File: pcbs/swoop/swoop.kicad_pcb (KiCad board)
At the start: 2 copper layers, 109.5 x 89.6 mm, 68 parts, among them J1 TRRS, SW1 Choc, SW10 Choc, SW11 Choc, SW12 Choc, SW13 Choc, SW14 Choc, SW15 Choc, SW16 Choc, SW17 Choc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

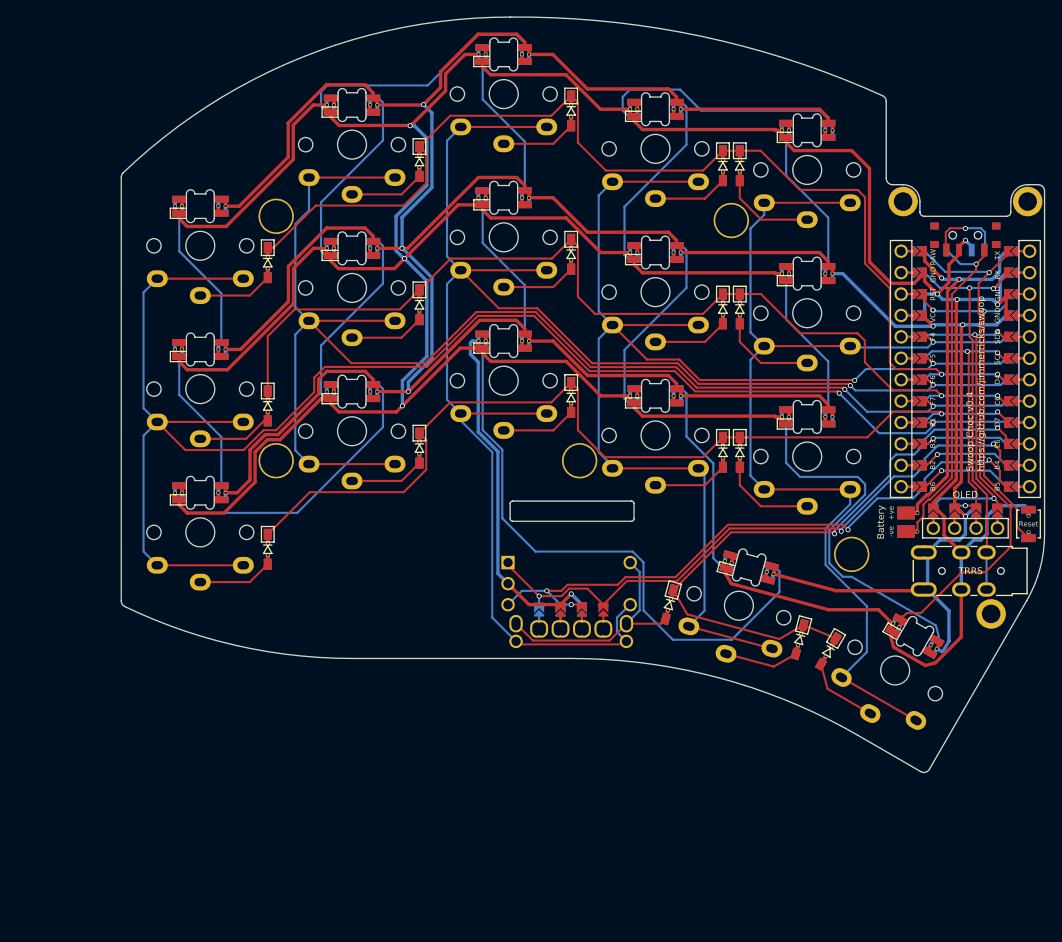
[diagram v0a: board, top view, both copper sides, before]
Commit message: Fixed the cover
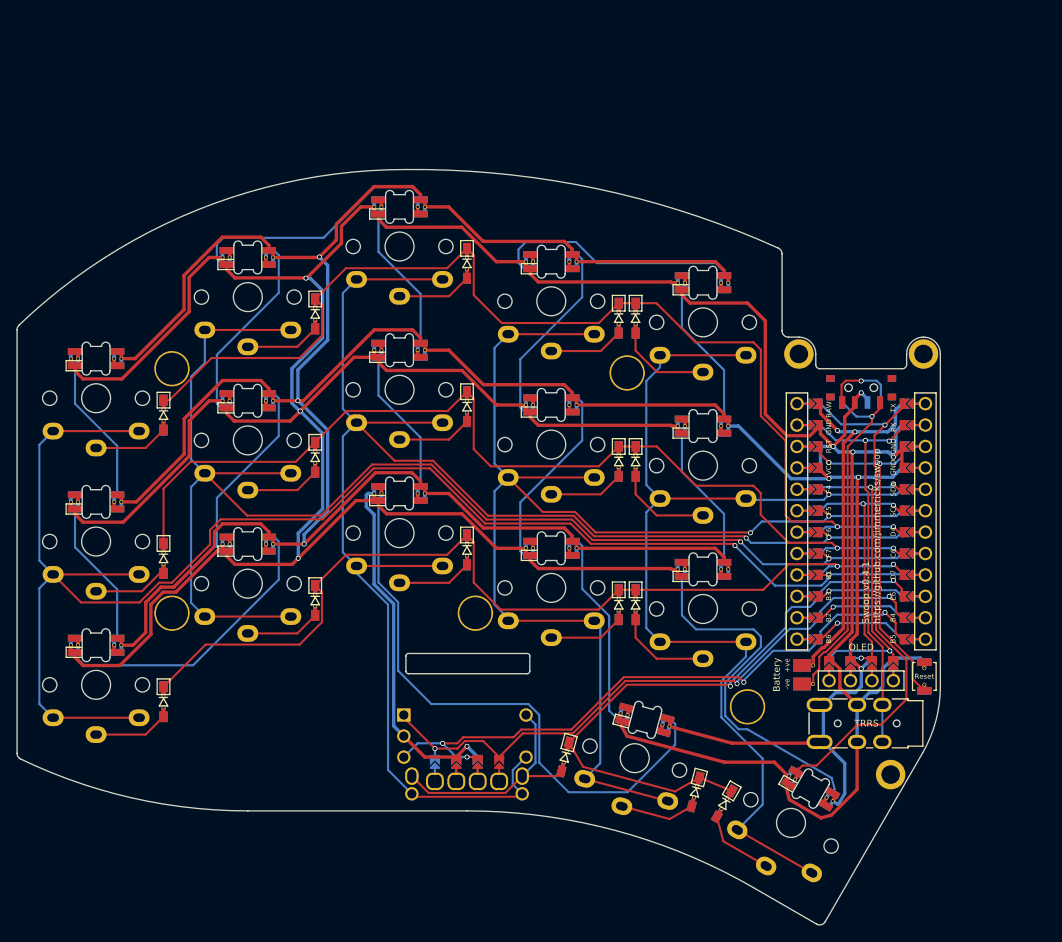
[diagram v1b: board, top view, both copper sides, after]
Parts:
- moved Ref** 22.5 mm to (165.5, 131.9)
- moved D4 21.9 mm to (133.2, 77.7)
- moved D13 21.9 mm to (115.2, 105.2)
- moved D7 21.9 mm to (97.2, 94.2)
- moved J1 21.9 mm to (167.7, 125.8)
- moved L1 21.9 mm to (71.2, 82.5)
- moved L13 21.9 mm to (107.2, 98.5)
- moved L14 21.9 mm to (125.2, 105.0)
- moved L7 21.9 mm to (89.2, 87.5)
- moved Ref** 21.9 mm to (154.6, 82.0)
- moved SW12 21.9 mm to (89.2, 109.2)
- moved SW5 21.9 mm to (143.2, 78.2)
- moved SW7 21.9 mm to (89.2, 92.2)
- moved U1 21.9 mm to (162.0, 101.9)
- moved D5 21.9 mm to (135.2, 77.7)
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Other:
- outline, holes or cut-outs redrawn
- board text added: "Swoop Choc v0.4.1 https://github.com/jimmerricks/swoop"
- board text added: "Swoop v0.4.1 https://github.com/jimmerricks/swoop"
- board text removed: "Swoop Choc v0.4 https://github.com/jimmerricks/swoop"
